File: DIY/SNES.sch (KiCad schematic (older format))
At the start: 6 parts, among them J1 Conn_01x07, J2 Conn_01x07, J3 DB25_Male, U1 74AHCT125N, U2 74AHCT125N, U3 74AHCT125N

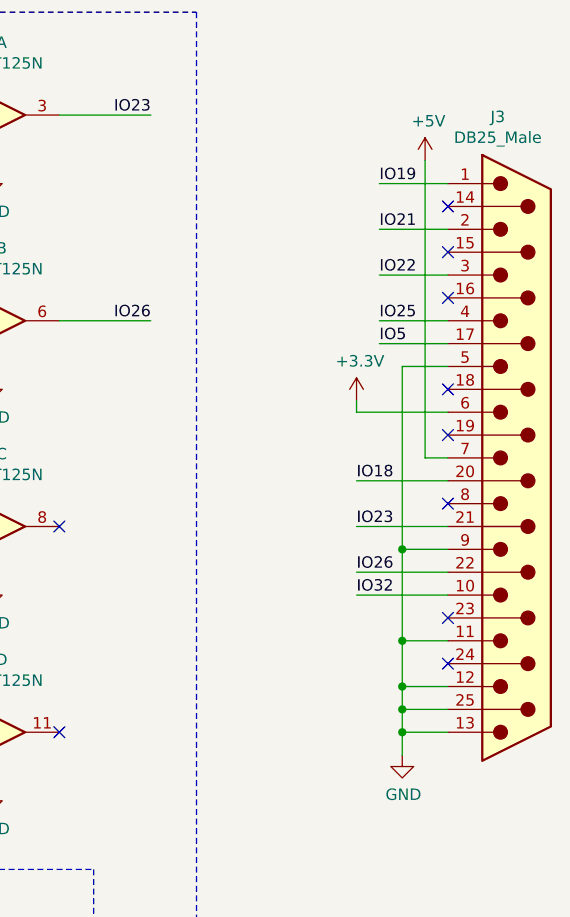
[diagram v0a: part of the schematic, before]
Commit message: [DIY] Update DIY & cable adapter schematic base on new DB25 mapping
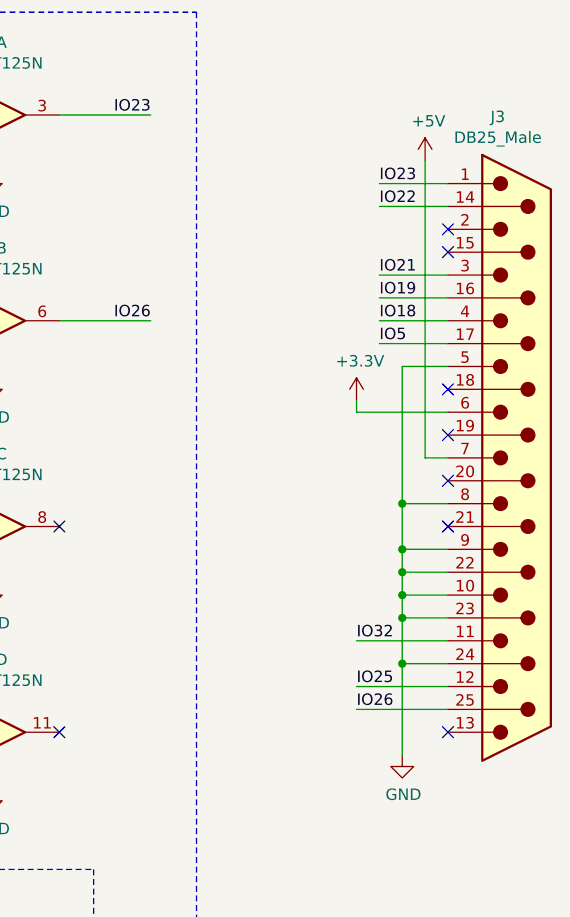
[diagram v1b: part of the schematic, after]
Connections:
- net GND: now also J3.10, J3.22 (P22), J3.23 (P23), J3.24 (P24), J3.8; no longer J3.11, J3.12, J3.13, J3.25 (P25)
- net IO18: now also J3.4; no longer J3.20 (P20)
- net IO19: now also J3.16 (P16); no longer J3.1
- net IO21: now also J3.3; no longer J3.2
- net IO22: now also J3.14 (P14); no longer J3.3
- net IO23: now also J3.1; no longer J3.21 (P21)
- net IO25: now also J3.12; no longer J3.4
- net IO26: now also J3.25 (P25); no longer J3.22 (P22)
- net IO32: now also J3.11; no longer J3.10
- no-connect marks 12 -> 11
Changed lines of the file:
@@
 $Descr USLetter 11000 8500
 encoding utf-8
-Sheet 4 4
+Sheet 4 7
 Title "BlueRetro - SFC/SNES adapter cable"
-Date "2020-08-04"
-Rev "v1.0"
+Date "2020-08-22"
+Rev "v1.1"
 Comp ""
 Comment1 ""
@@
 	9250 1550 9550 1550
 Wire Wire Line
-	9250 1750 9550 1750
-Wire Wire Line
 	9250 1950 9550 1950
 Wire Wire Line
@@
 Wire Wire Line
 	9550 3150 9350 3150
-Connection ~ 9350 3150
 Wire Wire Line
 	9450 1450 9450 2750
@@
 	1    0    0    -1
 $EndComp
-Text Label 9250 1550 0    50   ~ 0
+Text Label 9250 2050 0    50   ~ 0
 IO19
-Text Label 9250 1750 0    50   ~ 0
+Text Label 9250 1950 0    50   ~ 0
 IO21
-Text Label 9250 1950 0    50   ~ 0
+Text Label 9250 1650 0    50   ~ 0
 IO22
-Text Label 9250 2150 0    50   ~ 0
+Text Label 9150 3750 0    50   ~ 0
 IO25
 Wire Wire Line
@@
 Wire Wire Line
 	9150 2550 9550 2550
-Wire Wire Line
-	9150 2850 9550 2850
-NoConn ~ 9550 1850
-NoConn ~ 9550 2450
-NoConn ~ 9550 2650
-NoConn ~ 9550 2950
 Text Label 9250 2250 0    50   ~ 0
 IO5
-Text Label 9150 2850 0    50   ~ 0
+Text Label 9250 2150 0    50   ~ 0
 IO18
 Text Label 1850 3600 2    50   ~ 0
@@
 Text Label 1850 1950 2    50   ~ 0
 P1-D0
-Wire Wire Line
-	9550 3950 9350 3950
-Connection ~ 9350 3950
-Wire Wire Line
-	9350 3950 9350 4050
-Wire Wire Line
-	9550 3750 9350 3750
-Connection ~ 9350 3750
-Wire Wire Line
-	9350 3750 9350 3850
-Wire Wire Line
-	9550 3550 9350 3550
-Connection ~ 9350 3550
-Wire Wire Line
-	9350 3550 9350 3750
-Wire Wire Line
-	9550 3350 9150 3350
-Text Label 9150 3350 0    50   ~ 0
+Text Label 9150 3550 0    50   ~ 0
 IO32
-NoConn ~ 9550 1650
-NoConn ~ 9550 2050
-NoConn ~ 9550 3650
 Text Label 2900 1250 0    50   ~ 0
 IO19
@@
 $EndComp
 NoConn ~ 7850 3050
-NoConn ~ 9550 3450
-Wire Wire Line
-	9350 2350 9350 3150
-Wire Wire Line
-	9350 3150 9350 3550
-Wire Wire Line
-	9550 3050 9150 3050
-Wire Wire Line
-	9550 3250 9150 3250
-Text Label 9150 3050 0    50   ~ 0
+Wire Wire Line
+	9350 2350 9350 2950
+Text Label 9250 1550 0    50   ~ 0
 IO23
-Text Label 9150 3250 0    50   ~ 0
+Text Label 9150 3850 0    50   ~ 0
 IO26
 Wire Notes Line
@@
 Text Label 1850 4000 2    50   ~ 0
 P2-SEL
-Wire Wire Line
-	9550 3850 9350 3850
-Connection ~ 9350 3850
-Wire Wire Line
-	9350 3850 9350 3950
 Wire Notes Line
 	2850 1750 4200 1750
@@
 Text Notes 3150 4550 0    50   ~ 0
 * Only for Multitap support
+Wire Wire Line
+	9350 4050 9350 3650
+Connection ~ 9350 3150
+Wire Wire Line
+	9550 2950 9350 2950
+Connection ~ 9350 2950
+Wire Wire Line
+	9350 2950 9350 3150
+Wire Wire Line
+	9550 3250 9350 3250
+Connection ~ 9350 3250
+Wire Wire Line
+	9350 3250 9350 3150
+Wire Wire Line
+	9550 2050 9250 2050
+Wire Wire Line
+	9550 1650 9250 1650
+Wire Wire Line
+	9550 3750 9150 3750
+Wire Wire Line
+	9550 3550 9150 3550
+Wire Wire Line
+	9550 3850 9150 3850
+NoConn ~ 9550 3950
+NoConn ~ 9550 1750
+NoConn ~ 9550 1850
+NoConn ~ 9550 2450
+NoConn ~ 9550 2650
+NoConn ~ 9550 2850
+NoConn ~ 9550 3050
+Wire Wire Line
+	9550 3350 9350 3350
+Connection ~ 9350 3350
+Wire Wire Line
+	9350 3350 9350 3250
+Wire Wire Line
+	9550 3450 9350 3450
+Connection ~ 9350 3450
+Wire Wire Line
+	9350 3450 9350 3350
+Wire Wire Line
+	9550 3650 9350 3650
+Connection ~ 9350 3650
+Wire Wire Line
+	9350 3650 9350 3450
 $EndSCHEMATC

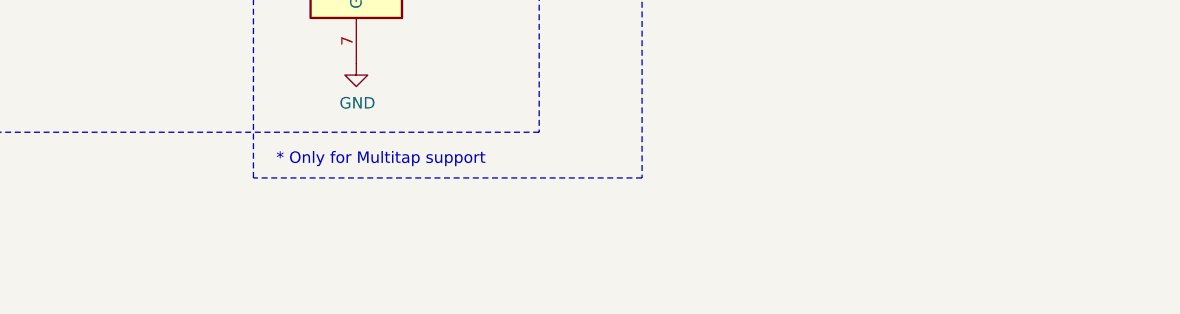
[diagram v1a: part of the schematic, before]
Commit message: [DIY] Add note to cable schematics to underline how important I39 is.
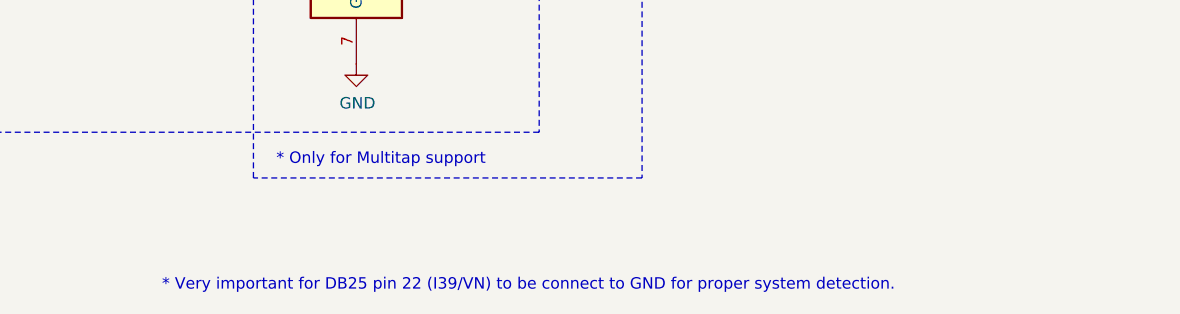
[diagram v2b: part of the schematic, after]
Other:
- note added: "* Very important for DB25 pin 22 (I39/VN) to be connect to GND for proper system detection."
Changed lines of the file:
@@
 Wire Wire Line
 	9350 3650 9350 3450
+Text Notes 6350 6900 0    50   ~ 0
+* Very important for DB25 pin 22 (I39/VN) to be connect to GND for proper system detection.
 $EndSCHEMATC

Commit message: Use new port symbol in cable schematic
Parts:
- J1, J2: symbol Connector_Generic:Conn_01x07 -> Connector_Gaming:SFC_SNES
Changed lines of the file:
@@
 Sheet 4 7
 Title "BlueRetro - SFC/SNES adapter cable"
-Date "2020-08-22"
-Rev "v1.1"
-Comp ""
+Date "2020-10-02"
+Rev "v1.2"
+Comp "©2020 Jacques Gagnon, licensed under CC-BY-4.0"
 Comment1 ""
 Comment2 ""
@@
 IO18
 $Comp
-L Connector_Generic:Conn_01x07 J?
+L Connector_Gaming:SFC_SNES J?
 U 1 1 5F2F19B9
-P 1150 1950
+P 1150 1850
 AR Path="/5F127084/5F2F19B9" Ref="J?"  Part="1"
 AR Path="/5F1E85DD/5F2F19B9" Ref="J?"  Part="1"
 AR Path="/5F2C5C0D/5F2F19B9" Ref="J1"  Part="1"
-F 0 "J1" H 1150 2500 50  0000 C CNN
-F 1 "Conn_01x07" H 1150 2400 50  0000 C CNN
-F 2 "" H 1150 1950 50  0001 C CNN
-F 3 "~" H 1150 1950 50  0001 C CNN
-	1    1150 1950
+F 0 "J1" H 1150 2200 50  0000 C CNN
+F 1 "Conn_01x07" H 1150 2300 50  0001 C CNN
+F 2 "" H 1150 1850 50  0001 C CNN
+F 3 "~" H 1150 1850 50  0001 C CNN
+	1    1150 1850
 	-1   0    0    -1
 $EndComp
 $Comp
-L Connector_Generic:Conn_01x07 J?
+L Connector_Gaming:SFC_SNES J?
 U 1 1 5F2F19BF
-P 1150 3800
+P 1150 3700
 AR Path="/5F127084/5F2F19BF" Ref="J?"  Part="1"
 AR Path="/5F1E85DD/5F2F19BF" Ref="J?"  Part="1"
 AR Path="/5F2C5C0D/5F2F19BF" Ref="J2"  Part="1"
-F 0 "J2" H 1150 4350 50  0000 C CNN
-F 1 "Conn_01x07" H 1150 4250 50  0000 C CNN
-F 2 "" H 1150 3800 50  0001 C CNN
-F 3 "~" H 1150 3800 50  0001 C CNN
-	1    1150 3800
+F 0 "J2" H 1150 4050 50  0000 C CNN
+F 1 "Conn_01x07" H 1150 4150 50  0001 C CNN
+F 2 "" H 1150 3700 50  0001 C CNN
+F 3 "~" H 1150 3700 50  0001 C CNN
+	1    1150 3700
 	-1   0    0    -1
 $EndComp

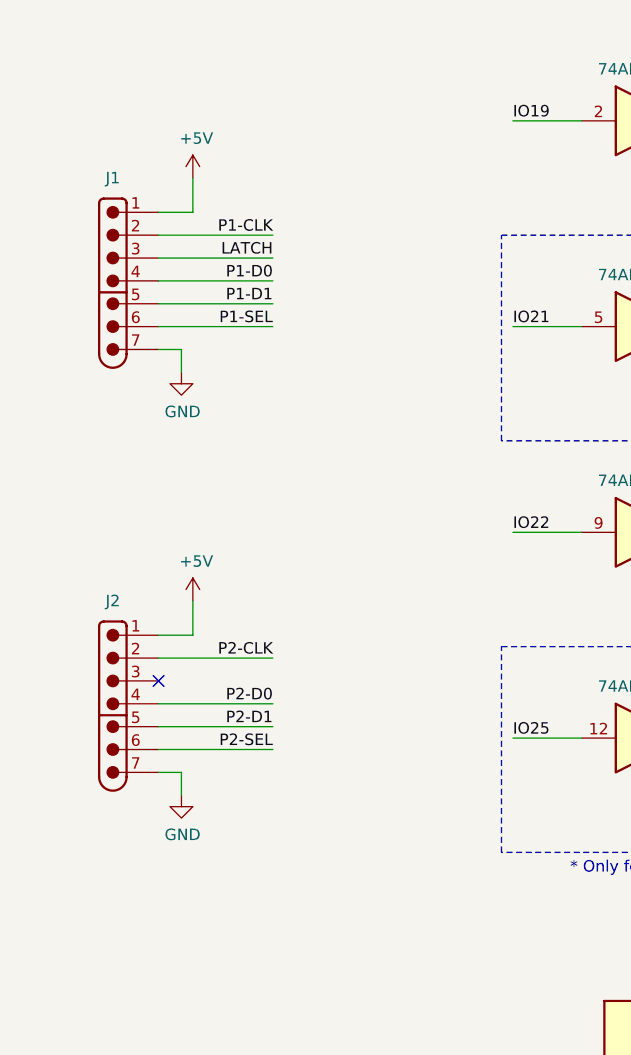
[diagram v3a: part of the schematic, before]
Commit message: Update adapter cable schematics
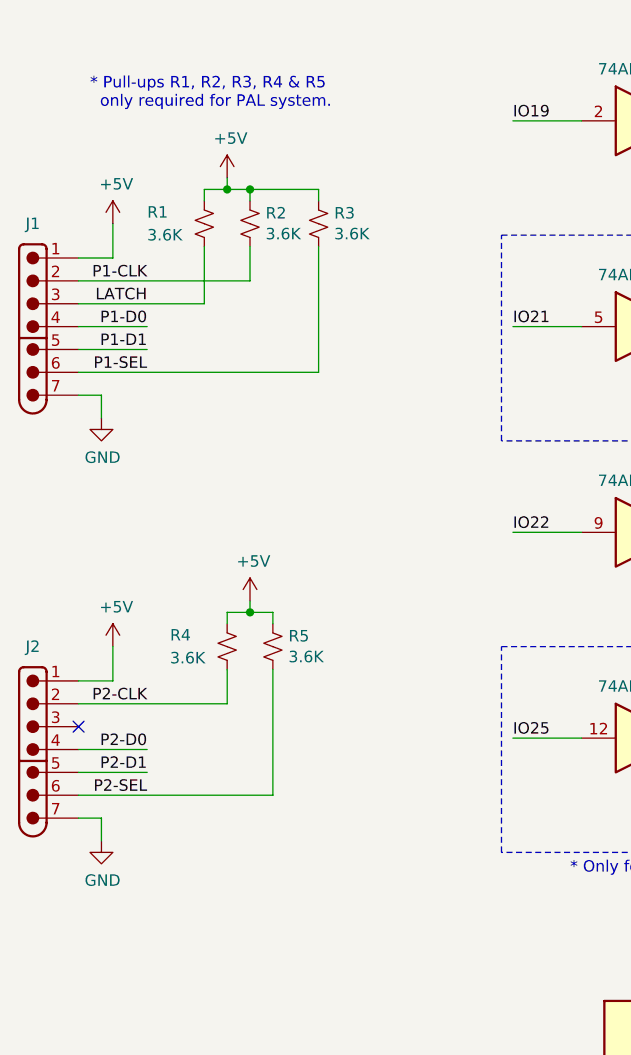
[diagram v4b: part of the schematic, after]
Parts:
- added R1, R2, R3, R4, R5: 3.6K, symbol Device:R_Small_US
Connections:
- net +5V: now also R1.1, R2.1, R3.1, R4.1, R5.1
- net LATCH: now also R1.2
- net P1-CLK: now also R2.2
- net P1-SEL: now also R3.2
- net P2-CLK: now also R4.2
- net P2-SEL: now also R5.2
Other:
- note added: "* Pull-ups R1, R2, R3, R4 & R5 \n only required for PAL system."
- moved on the sheet: J1, J2
